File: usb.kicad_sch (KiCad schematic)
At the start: 104 parts, among them J901 USB-C_GCT_USB4105-GF-A, J902 USB-C_GCT_USB4105-GF-A, Q901 PJE138K, Q902 SQS401EN-T1_BE3, Q903 SSM3J332R, Q904 PJE138K, T901 Choke_DLW21SN900SQ2L, T902 Choke_DLW21SN900SQ2L, U901 AP22615A_TSOT26, U902 93AA66C, U903 AP62301WU-7, U905 FT4233HPQ, U906 TUSB321RWBR, Y901 Oscillator_SMD_12MHz_KX-7

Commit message: [#53901] Update symbols & footprints from lib
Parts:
- C929: Val 330u/6.3V -> 330u
- D905, D906, D907, D912: footprint antmicro-footprints:LED_0603_1608Metric_R -> antmicro-footprints:LED_0603_1608Metric_G; symbol antmicroLEDIndicationDiscrete:LED_R_0603_598-8D80-107F -> antmicroLEDIndicationDiscrete:LED_G_0603_598-8D80-107F
- FB901, FB902, FB903: value FB_120Z_1.3A_0402 -> FB_120Z_1.3A_Murata-BLM15PD_0402
- L901: value L_1u_5.5A_SRP3212 -> L_1u_5.5A_Bourns-SRP3212A; MaxCur 5.5A -> (none)
- Q902, TP901, TP902, TP903, TP905, TP906, TP907, TP908, TP909, TP910, TP911, TP912, TP913, TP914, TP915, TP916, TP917: now left out of the parts list
- R908, R911: DNP DNP -> (none); now in the parts list
- U902: value 93AA66C -> 93AA66C_SOIC
- U903: value AP62301WU-7 -> AP62301_TSOT
- Y901: value Oscillator_SMD_12MHz_KX-7 -> Resonator_12MHz_ABM8G

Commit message: [#56708] Add loclib
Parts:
- C901, C902, C903, C904, C906, C909, C910, C912, C913, C914, C915, C916, C917, C918, C919, C920, C921, C922, C923, C928, C930: footprint antmicro-footprints:C_0402_1005Metric -> cm4-baseboard-footprints:C_0402_1005Metric; symbol antmicroCapacitors0402:C_100n_0402 -> cm4-baseboard:C_100n_0402
- C905, C907, C911, C932: footprint antmicro-footprints:C_0805_2012Metric -> cm4-baseboard-footprints:C_0805_2012Metric; symbol antmicroCapacitorsmisc:C_22u_25V_0805 -> cm4-baseboard:C_22u_25V_0805
- C908: footprint antmicro-footprints:C_0402_1005Metric -> cm4-baseboard-footprints:C_0402_1005Metric; symbol antmicroCapacitors0402:C_10u_0402 -> cm4-baseboard:C_10u_0402
- C924, C925: footprint antmicro-footprints:C_0402_1005Metric -> cm4-baseboard-footprints:C_0402_1005Metric; symbol antmicroCapacitors0402:C_4u7_0402 -> cm4-baseboard:C_4u7_0402
- C926, C927: footprint antmicro-footprints:C_0402_1005Metric -> cm4-baseboard-footprints:C_0402_1005Metric; symbol antmicroCapacitors0402:C_18p_0402 -> cm4-baseboard:C_18p_0402
- C929: footprint antmicro-footprints:C_Pol_EIA-B -> cm4-baseboard-footprints:C_Pol_EIA-B; symbol antmicroCapacitorspol:C_Pol_330u_6.3V_KEMET-T520-B -> cm4-baseboard:C_Pol_330u_6.3V_KEMET-T520-B
- C931: footprint antmicro-footprints:C_0402_1005Metric -> cm4-baseboard-footprints:C_0402_1005Metric; symbol antmicroCapacitors0402:C_1u_25V_0402 -> cm4-baseboard:C_1u_25V_0402
- D901, D902: footprint antmicro-footprints:Nexperia_DFN-10_2.5x1mm_P0.5mm -> cm4-baseboard-footprints:Nexperia_DFN-10_2.5x1mm_P0.5mm; symbol antmicroTVSDiodes:PUSB3F96X_PASS -> cm4-baseboard:PUSB3F96X_PASS
- D903: footprint antmicro-footprints:SOD-523 -> cm4-baseboard-footprints:SOD-523; symbol antmicroTVSDiodes:PESD5Z5_0F -> cm4-baseboard:PESD5Z5_0F
- D904: footprint antmicro-footprints:SOD-123FL -> cm4-baseboard-footprints:SOD-123FL; symbol antmicroTVSDiodes:SMF4L15A -> cm4-baseboard:SMF4L15A
- D905, D906, D907, D912: footprint antmicro-footprints:LED_0603_1608Metric_G -> cm4-baseboard-footprints:LED_0603_1608Metric_G; symbol antmicroLEDIndicationDiscrete:LED_G_0603_598-8D80-107F -> cm4-baseboard:LED_G_0603_598-8D80-107F
- D910: footprint antmicro-footprints:SOD-523 -> cm4-baseboard-footprints:SOD-523; symbol antmicroDiodesRectifiersSingle:RB521S30T1G -> cm4-baseboard:RB521S30T1G
- D911: footprint antmicro-footprints:LED_0402_1005Metric_Y -> cm4-baseboard-footprints:LED_0402_1005Metric_Y; symbol antmicroLEDIndicationDiscrete:LED_Y_0402_VLMY1500-GS08 -> cm4-baseboard:LED_Y_0402_VLMY1500-GS08
- FB901, FB902, FB903: footprint antmicro-footprints:FB_0402_1005Metric -> cm4-baseboard-footprints:FB_0402_1005Metric; symbol antmicroFerriteBeadsandChips:FB_120Z_1.3A_Murata-BLM15PD_0402 -> cm4-baseboard:FB_120Z_1.3A_Murata-BLM15PD_0402
- J901, J902: footprint antmicro-footprints:USB-C_Receptacle_GCT_USB4105-GF-A -> cm4-baseboard-footprints:USB-C_Receptacle_GCT_USB4105-GF-A; symbol antmicroUSBConnectors:USB-C_GCT_USB4105-GF-A -> cm4-baseboard:USB-C_GCT_USB4105-GF-A
- L901: footprint antmicro-footprints:L_Bourns-SRP3212A -> cm4-baseboard-footprints:L_Bourns-SRP3212A; symbol antmicroFixedInductors:L_1u_5.5A_Bourns-SRP3212A -> cm4-baseboard:L_1u_5.5A_Bourns-SRP3212A
- Q901, Q904: footprint antmicro-footprints:SOT-523 -> cm4-baseboard-footprints:SOT-523; symbol antmicroTransistorsFETsMOSFETsSingle:PJE138K -> cm4-baseboard:PJE138K
- Q902: footprint antmicro-footprints:Vishay_PowerPAK_1212-8_Single -> cm4-baseboard-footprints:Vishay_PowerPAK_1212-8_Single; symbol antmicroTransistorsFETsMOSFETsSingle:SQS401EN-T1_BE3 -> cm4-baseboard:SQS401EN-T1_BE3
- Q903: footprint antmicro-footprints:SOT-23-3 -> cm4-baseboard-footprints:SOT-23-3; symbol antmicroTransistorsFETsMOSFETsSingle:SSM3J332R -> cm4-baseboard:SSM3J332R
- R901, R902, R923: footprint antmicro-footprints:R_0402_1005Metric -> cm4-baseboard-footprints:R_0402_1005Metric; symbol antmicroResistors0402:R_1k_0402 -> cm4-baseboard:R_1k_0402
- R903: footprint antmicro-footprints:R_0402_1005Metric -> cm4-baseboard-footprints:R_0402_1005Metric; symbol antmicroResistors0402:R_910k_0402 -> cm4-baseboard:R_910k_0402
- R904, R914, R916, R925: footprint antmicro-footprints:R_0402_1005Metric -> cm4-baseboard-footprints:R_0402_1005Metric; symbol antmicroResistors0402:R_100k_0402 -> cm4-baseboard:R_100k_0402
- R905, R927: footprint antmicro-footprints:R_0402_1005Metric -> cm4-baseboard-footprints:R_0402_1005Metric; symbol antmicroResistors0402:R_4k7_0402 -> cm4-baseboard:R_4k7_0402
- R906, R908, R909, R910, R911, R924, R928: footprint antmicro-footprints:R_0402_1005Metric -> cm4-baseboard-footprints:R_0402_1005Metric; symbol antmicroResistors0402:R_10k_0402 -> cm4-baseboard:R_10k_0402
- R907, R913: footprint antmicro-footprints:R_0402_1005Metric -> cm4-baseboard-footprints:R_0402_1005Metric; symbol antmicroResistors0402:R_2k2_0402 -> cm4-baseboard:R_2k2_0402
- R912: footprint antmicro-footprints:R_0402_1005Metric -> cm4-baseboard-footprints:R_0402_1005Metric; symbol antmicroResistors0402:R_6k8_0402 -> cm4-baseboard:R_6k8_0402
- R915: footprint antmicro-footprints:R_0402_1005Metric -> cm4-baseboard-footprints:R_0402_1005Metric; symbol antmicroResistors0402:R_470k_0402 -> cm4-baseboard:R_470k_0402
- R917: footprint antmicro-footprints:R_0402_1005Metric -> cm4-baseboard-footprints:R_0402_1005Metric; symbol antmicroResistors0402:R_15k_0402 -> cm4-baseboard:R_15k_0402
- R918: footprint antmicro-footprints:R_0402_1005Metric -> cm4-baseboard-footprints:R_0402_1005Metric; symbol antmicroResistors0402:R_200R_0402 -> cm4-baseboard:R_200R_0402
- R919: footprint antmicro-footprints:R_0402_1005Metric -> cm4-baseboard-footprints:R_0402_1005Metric; symbol antmicroResistors0402:R_0R_0402 -> cm4-baseboard:R_0R_0402
- R920: footprint antmicro-footprints:R_0402_1005Metric -> cm4-baseboard-footprints:R_0402_1005Metric; symbol antmicroResistors0402:R_470R_0402 -> cm4-baseboard:R_470R_0402
- R921, R926: footprint antmicro-footprints:R_0402_1005Metric -> cm4-baseboard-footprints:R_0402_1005Metric; symbol antmicroResistors0402:R_100R_0402 -> cm4-baseboard:R_100R_0402
- R922: footprint antmicro-footprints:R_0402_1005Metric -> cm4-baseboard-footprints:R_0402_1005Metric; symbol antmicroResistors0402:R_12k_0402 -> cm4-baseboard:R_12k_0402
- T901, T902: footprint antmicro-footprints:Choke_Murata-DLW21 -> cm4-baseboard-footprints:Choke_Murata-DLW21; symbol antmicroCommonModeChokes:Choke_DLW21SN900SQ2L -> cm4-baseboard:Choke_DLW21SN900SQ2L
- TP901, TP902, TP903, TP905, TP906, TP907, TP908, TP909, TP910, TP911, TP912, TP913, TP914, TP915, TP916, TP917: footprint antmicro-footprints:TP_SMD_0.75mm -> cm4-baseboard-footprints:TP_SMD_0.75mm; symbol antmicroTestPoints:TP_0.75mm_SMD -> cm4-baseboard:TP_0.75mm_SMD
- U901: footprint antmicro-footprints:TSOT23-6 -> cm4-baseboard-footprints:TSOT23-6; symbol antmicroPMICPowerDistributionSwitchesLoadDrivers:AP22615A_TSOT26 -> cm4-baseboard:AP22615A_TSOT26
- U902: footprint antmicro-footprints:SOIC-8_3.9x4.9x1.75mm_P1.27mm -> cm4-baseboard-footprints:SOIC-8_3.9x4.9x1.75mm_P1.27mm; symbol antmicroMemory:93AA66C_SOIC -> cm4-baseboard:93AA66C_SOIC
- U903: footprint antmicro-footprints:TSOT23-6 -> cm4-baseboard-footprints:TSOT23-6; symbol antmicroDCDCConverters:AP62301_TSOT -> cm4-baseboard:AP62301_TSOT
- U905: footprint antmicro-footprints:QFN-76-1EP_9x9mm_P0.4mm_EP6.3x6.3mm -> cm4-baseboard-footprints:QFN-76-1EP_9x9mm_P0.4mm_EP6.3x6.3mm; symbol antmicroInterfaceControllers:FT4233HPQ -> cm4-baseboard:FT4233HPQ
- U906: footprint antmicro-footprints:Texas_X2QFN-12_1.6x1.6mm_P0.4mm -> cm4-baseboard-footprints:Texas_X2QFN-12_1.6x1.6mm_P0.4mm; symbol antmicroInterfaceControllers:TUSB321RWBR -> cm4-baseboard:TUSB321RWBR
- Y901: footprint antmicro-footprints:Oscillator_SMD_Geyer_KX-7-4Pin_3.2x2.5mm -> cm4-baseboard-footprints:Oscillator_SMD_Geyer_KX-7-4Pin_3.2x2.5mm; symbol antmicroResonators:Resonator_12MHz_ABM8G -> cm4-baseboard:Resonator_12MHz_ABM8G

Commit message: [#56708] Update symbol/footprint props; Update modules visibilty
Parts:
- D905, D906, D907, D912: value LED_G -> LED_G_0603_598-8D80-107F; Color (none) -> Green
- D911: value LED_Y -> LED_Y_0402_VLMY1500-GS08; Color (none) -> Yellow; VSD_class LED -> (none)
- Q902: now in the parts list
- R908, R911: DNP (none) -> DNP; now left out of the parts list
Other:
- moved on the sheet: R902

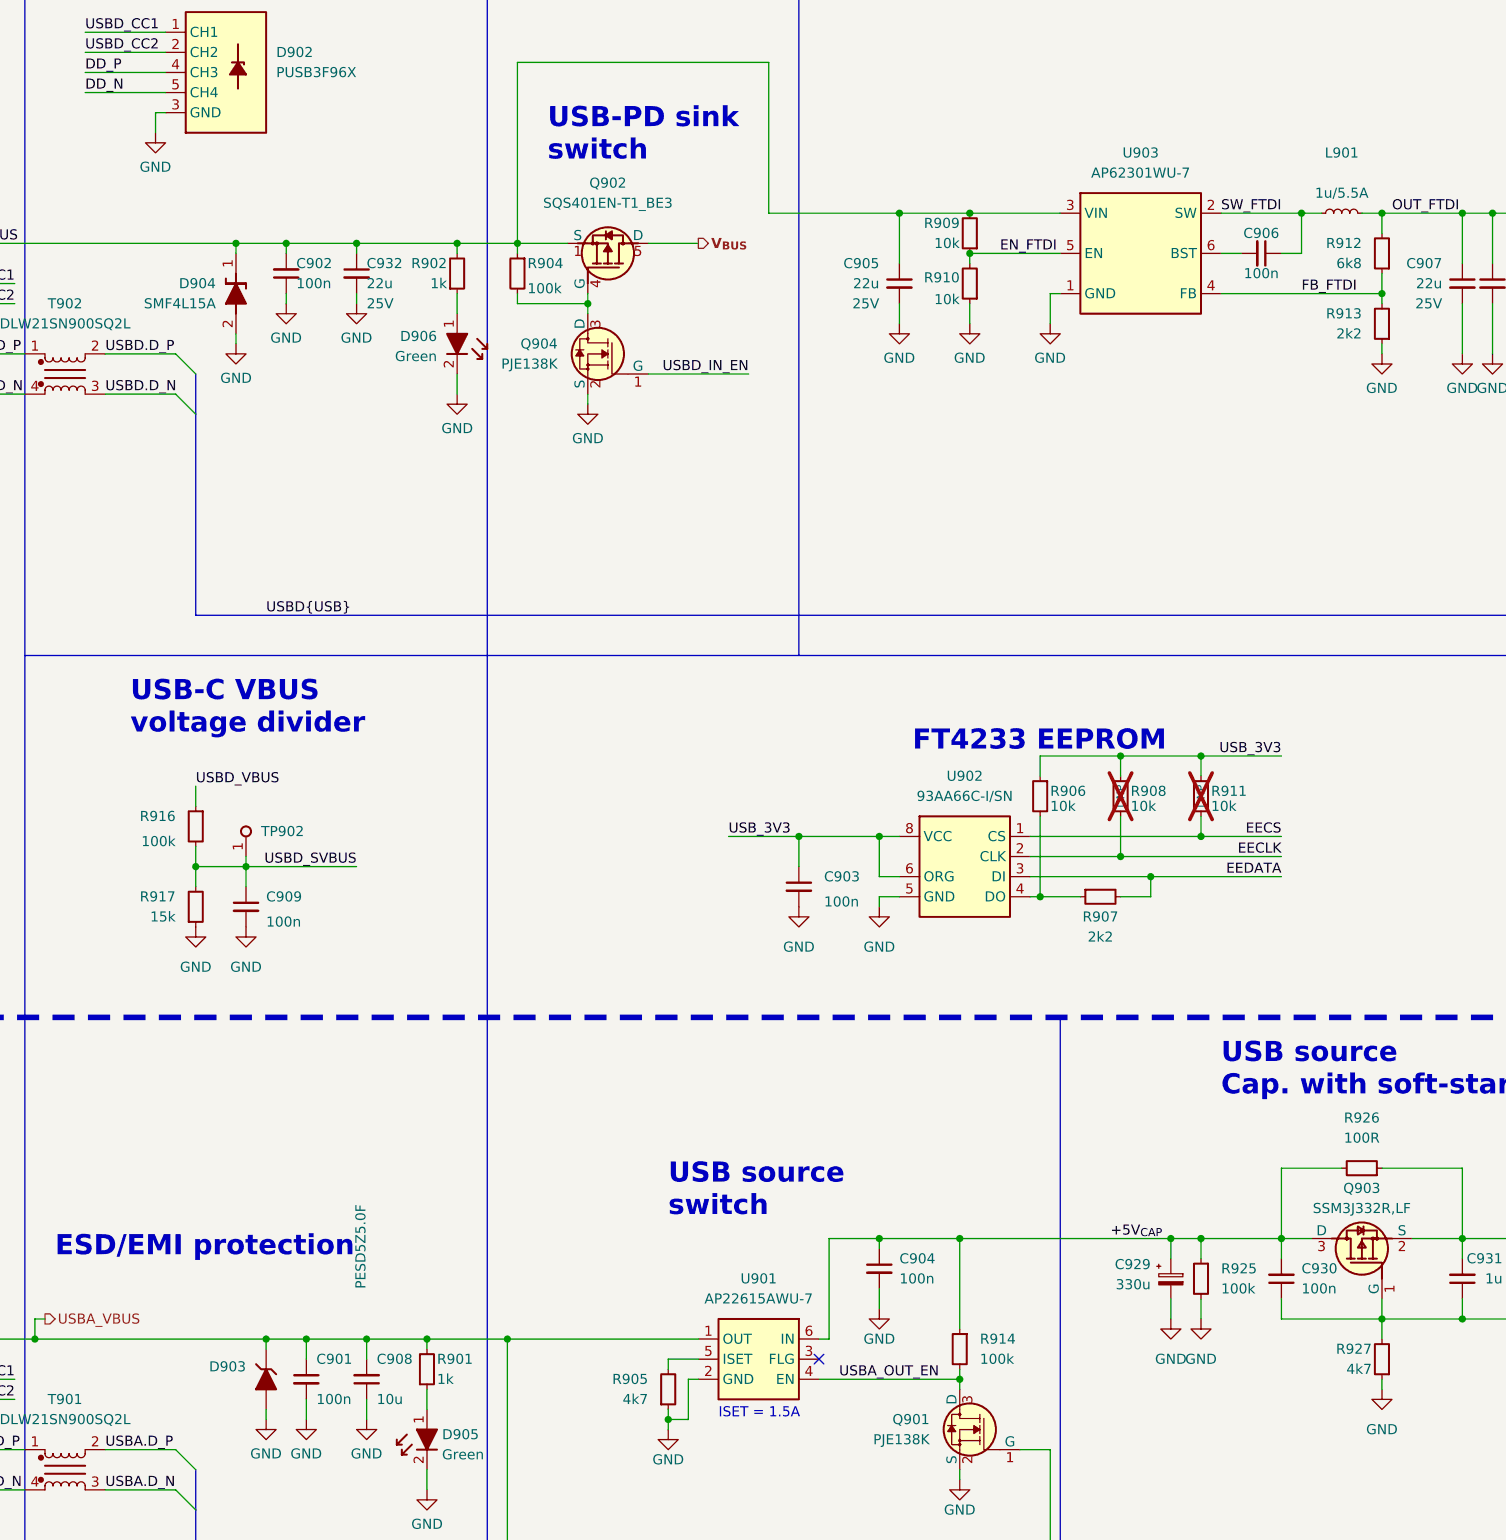
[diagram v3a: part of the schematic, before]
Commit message: [#57456] Remove loclib
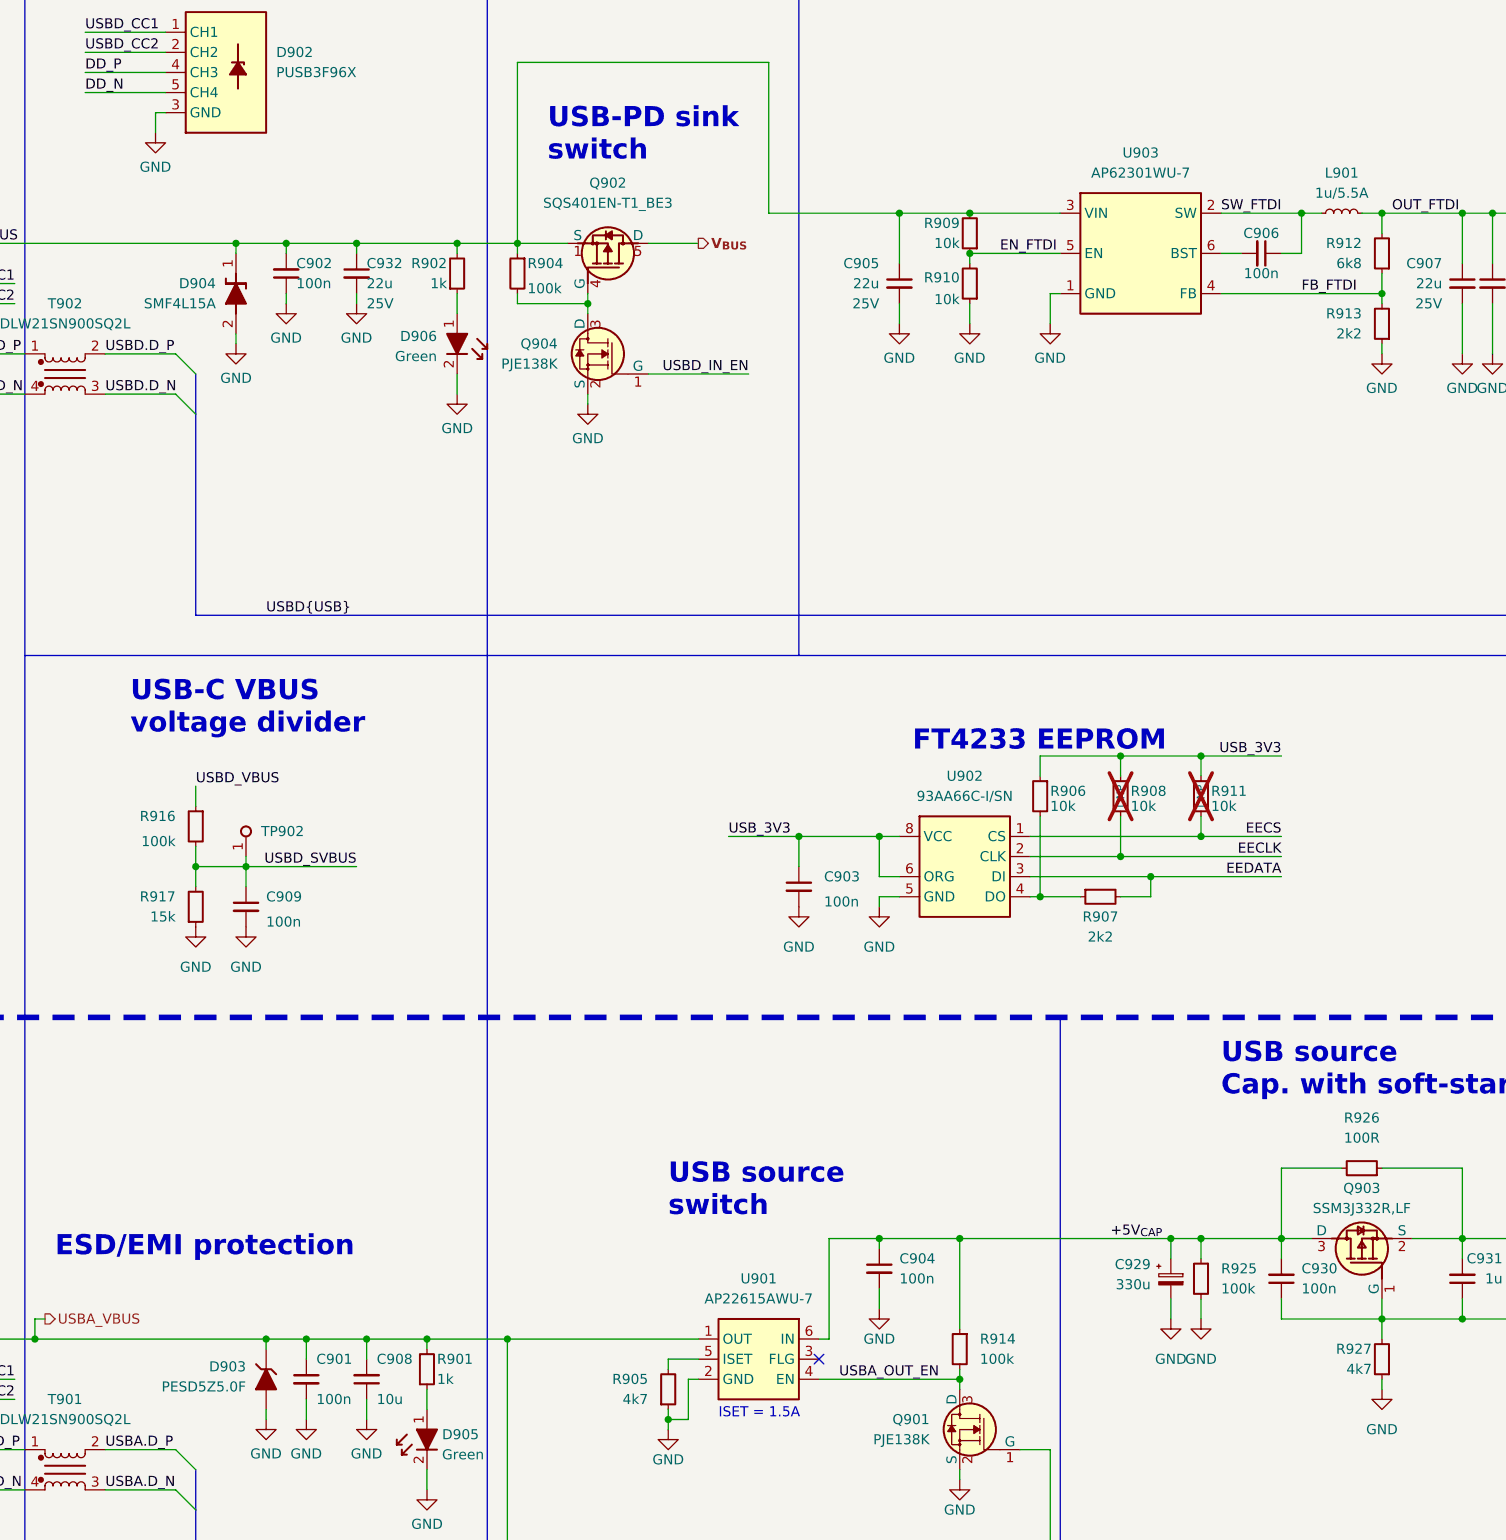
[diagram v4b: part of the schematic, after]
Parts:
- C901, C902, C903, C904, C906, C909, C910, C912, C913, C914, C915, C916, C917, C918, C919, C920, C921, C922, C923, C928, C930: footprint cm4-baseboard-footprints:C_0402_1005Metric -> antmicro-footprints:C_0402_1005Metric; symbol cm4-baseboard:C_100n_0402 -> antmicroCapacitors0402:C_100n_0402
- C905, C907, C911, C932: footprint cm4-baseboard-footprints:C_0805_2012Metric -> antmicro-footprints:C_0805_2012Metric; symbol cm4-baseboard:C_22u_25V_0805 -> antmicroCapacitorsmisc:C_22u_25V_0805
- C908: footprint cm4-baseboard-footprints:C_0402_1005Metric -> antmicro-footprints:C_0402_1005Metric; symbol cm4-baseboard:C_10u_0402 -> antmicroCapacitors0402:C_10u_0402
- C924, C925: footprint cm4-baseboard-footprints:C_0402_1005Metric -> antmicro-footprints:C_0402_1005Metric; symbol cm4-baseboard:C_4u7_0402 -> antmicroCapacitors0402:C_4u7_0402
- C926, C927: footprint cm4-baseboard-footprints:C_0402_1005Metric -> antmicro-footprints:C_0402_1005Metric; symbol cm4-baseboard:C_18p_0402 -> antmicroCapacitors0402:C_18p_0402
- C929: footprint cm4-baseboard-footprints:C_Pol_EIA-B -> antmicro-footprints:C_Pol_EIA-B; symbol cm4-baseboard:C_Pol_330u_6.3V_KEMET-T520-B -> antmicroCapacitorspol:C_Pol_330u_6.3V_KEMET-T520-B
- C931: footprint cm4-baseboard-footprints:C_0402_1005Metric -> antmicro-footprints:C_0402_1005Metric; symbol cm4-baseboard:C_1u_25V_0402 -> antmicroCapacitors0402:C_1u_25V_0402
- D901, D902: footprint cm4-baseboard-footprints:Nexperia_DFN-10_2.5x1mm_P0.5mm -> antmicro-footprints:Nexperia_DFN-10_2.5x1mm_P0.5mm; symbol cm4-baseboard:PUSB3F96X_PASS -> antmicroTVSDiodes:PUSB3F96X_PASS
- D903: footprint cm4-baseboard-footprints:SOD-523 -> antmicro-footprints:SOD-523; symbol cm4-baseboard:PESD5Z5_0F -> antmicroTVSDiodes:PESD5Z5_0F
- D904: footprint cm4-baseboard-footprints:SOD-123FL -> antmicro-footprints:SOD-123FL; symbol cm4-baseboard:SMF4L15A -> antmicroTVSDiodes:SMF4L15A
- D905, D906, D907, D912: footprint cm4-baseboard-footprints:LED_0603_1608Metric_G -> antmicro-footprints:LED_0603_1608Metric_G; symbol cm4-baseboard:LED_G_0603_598-8D80-107F -> antmicroLEDIndicationDiscrete:LED_G_0603_598-8D80-107F
- D910: footprint cm4-baseboard-footprints:SOD-523 -> antmicro-footprints:SOD-523; symbol cm4-baseboard:RB521S30T1G -> antmicroDiodesRectifiersSingle:RB521S30T1G
- D911: footprint cm4-baseboard-footprints:LED_0402_1005Metric_Y -> antmicro-footprints:LED_0402_1005Metric_Y; symbol cm4-baseboard:LED_Y_0402_VLMY1500-GS08 -> antmicroLEDIndicationDiscrete:LED_Y_0402_VLMY1500-GS08
- FB901, FB902, FB903: footprint cm4-baseboard-footprints:FB_0402_1005Metric -> antmicro-footprints:FB_0402_1005Metric; symbol cm4-baseboard:FB_120Z_1.3A_Murata-BLM15PD_0402 -> antmicroFerriteBeadsandChips:FB_120Z_1.3A_Murata-BLM15PD_0402
- J901, J902: footprint cm4-baseboard-footprints:USB-C_Receptacle_GCT_USB4105-GF-A -> antmicro-footprints:USB-C_Receptacle_GCT_USB4105-GF-A; symbol cm4-baseboard:USB-C_GCT_USB4105-GF-A -> antmicroUSBConnectors:USB-C_GCT_USB4105-GF-A
- L901: footprint cm4-baseboard-footprints:L_Bourns-SRP3212A -> antmicro-footprints:L_Bourns-SRP3212A; symbol cm4-baseboard:L_1u_5.5A_Bourns-SRP3212A -> antmicroFixedInductors:L_1u_5.5A_Bourns-SRP3212A
- Q901, Q904: footprint cm4-baseboard-footprints:SOT-523 -> antmicro-footprints:SOT-523; symbol cm4-baseboard:PJE138K -> antmicroTransistorsFETsMOSFETsSingle:PJE138K
- Q902: footprint cm4-baseboard-footprints:Vishay_PowerPAK_1212-8_Single -> antmicro-footprints:Vishay_PowerPAK_1212-8_Single; symbol cm4-baseboard:SQS401EN-T1_BE3 -> antmicroTransistorsFETsMOSFETsSingle:SQS401EN-T1_BE3
- Q903: footprint cm4-baseboard-footprints:SOT-23-3 -> antmicro-footprints:SOT-23-3; symbol cm4-baseboard:SSM3J332R -> antmicroTransistorsFETsMOSFETsSingle:SSM3J332R
- R901, R902, R923: footprint cm4-baseboard-footprints:R_0402_1005Metric -> antmicro-footprints:R_0402_1005Metric; symbol cm4-baseboard:R_1k_0402 -> antmicroResistors0402:R_1k_0402
- R903: footprint cm4-baseboard-footprints:R_0402_1005Metric -> antmicro-footprints:R_0402_1005Metric; symbol cm4-baseboard:R_910k_0402 -> antmicroResistors0402:R_910k_0402
- R904, R914, R916, R925: footprint cm4-baseboard-footprints:R_0402_1005Metric -> antmicro-footprints:R_0402_1005Metric; symbol cm4-baseboard:R_100k_0402 -> antmicroResistors0402:R_100k_0402
- R905, R927: footprint cm4-baseboard-footprints:R_0402_1005Metric -> antmicro-footprints:R_0402_1005Metric; symbol cm4-baseboard:R_4k7_0402 -> antmicroResistors0402:R_4k7_0402
- R906, R908, R909, R910, R911, R924, R928: footprint cm4-baseboard-footprints:R_0402_1005Metric -> antmicro-footprints:R_0402_1005Metric; symbol cm4-baseboard:R_10k_0402 -> antmicroResistors0402:R_10k_0402
- R907, R913: footprint cm4-baseboard-footprints:R_0402_1005Metric -> antmicro-footprints:R_0402_1005Metric; symbol cm4-baseboard:R_2k2_0402 -> antmicroResistors0402:R_2k2_0402
- R912: footprint cm4-baseboard-footprints:R_0402_1005Metric -> antmicro-footprints:R_0402_1005Metric; symbol cm4-baseboard:R_6k8_0402 -> antmicroResistors0402:R_6k8_0402
- R915: footprint cm4-baseboard-footprints:R_0402_1005Metric -> antmicro-footprints:R_0402_1005Metric; symbol cm4-baseboard:R_470k_0402 -> antmicroResistors0402:R_470k_0402
- R917: footprint cm4-baseboard-footprints:R_0402_1005Metric -> antmicro-footprints:R_0402_1005Metric; symbol cm4-baseboard:R_15k_0402 -> antmicroResistors0402:R_15k_0402
- R918: footprint cm4-baseboard-footprints:R_0402_1005Metric -> antmicro-footprints:R_0402_1005Metric; symbol cm4-baseboard:R_200R_0402 -> antmicroResistors0402:R_200R_0402
- R919: footprint cm4-baseboard-footprints:R_0402_1005Metric -> antmicro-footprints:R_0402_1005Metric; symbol cm4-baseboard:R_0R_0402 -> antmicroResistors0402:R_0R_0402
- R920: footprint cm4-baseboard-footprints:R_0402_1005Metric -> antmicro-footprints:R_0402_1005Metric; symbol cm4-baseboard:R_470R_0402 -> antmicroResistors0402:R_470R_0402
- R921, R926: footprint cm4-baseboard-footprints:R_0402_1005Metric -> antmicro-footprints:R_0402_1005Metric; symbol cm4-baseboard:R_100R_0402 -> antmicroResistors0402:R_100R_0402
- R922: footprint cm4-baseboard-footprints:R_0402_1005Metric -> antmicro-footprints:R_0402_1005Metric; symbol cm4-baseboard:R_12k_0402 -> antmicroResistors0402:R_12k_0402
- T901, T902: footprint cm4-baseboard-footprints:Choke_Murata-DLW21 -> antmicro-footprints:Choke_Murata-DLW21; symbol cm4-baseboard:Choke_DLW21SN900SQ2L -> antmicroCommonModeChokes:Choke_DLW21SN900SQ2L
- TP901, TP902, TP903, TP905, TP906, TP907, TP908, TP909, TP910, TP911, TP912, TP913, TP914, TP915, TP916, TP917: footprint cm4-baseboard-footprints:TP_SMD_0.75mm -> antmicro-footprints:TP_SMD_0.75mm; symbol cm4-baseboard:TP_0.75mm_SMD -> antmicroTestPoints:TP_0.75mm_SMD
- U901: footprint cm4-baseboard-footprints:TSOT23-6 -> antmicro-footprints:TSOT23-6; symbol cm4-baseboard:AP22615A_TSOT26 -> antmicroPMICPowerDistributionSwitchesLoadDrivers:AP22615A_TSOT26
- U902: footprint cm4-baseboard-footprints:SOIC-8_3.9x4.9x1.75mm_P1.27mm -> antmicro-footprints:SOIC-8_3.9x4.9x1.75mm_P1.27mm; symbol cm4-baseboard:93AA66C_SOIC -> antmicroMemory:93AA66C_SOIC
- U903: footprint cm4-baseboard-footprints:TSOT23-6 -> antmicro-footprints:TSOT23-6; symbol cm4-baseboard:AP62301_TSOT -> antmicroDCDCConverters:AP62301_TSOT
- U905: footprint cm4-baseboard-footprints:QFN-76-1EP_9x9mm_P0.4mm_EP6.3x6.3mm -> antmicro-footprints:QFN-76-1EP_9x9mm_P0.4mm_EP6.3x6.3mm; symbol cm4-baseboard:FT4233HPQ -> antmicroInterfaceControllers:FT4233HPQ
- U906: footprint cm4-baseboard-footprints:Texas_X2QFN-12_1.6x1.6mm_P0.4mm -> antmicro-footprints:Texas_X2QFN-12_1.6x1.6mm_P0.4mm; symbol cm4-baseboard:TUSB321RWBR -> antmicroInterfaceControllers:TUSB321RWBR
- Y901: footprint cm4-baseboard-footprints:Oscillator_SMD_Geyer_KX-7-4Pin_3.2x2.5mm -> antmicro-footprints:Resonator_SMD_Abracon_ABM8G_3.2x2.5mm; symbol cm4-baseboard:Resonator_12MHz_ABM8G -> antmicroResonators:Resonator_12MHz_ABM8G
